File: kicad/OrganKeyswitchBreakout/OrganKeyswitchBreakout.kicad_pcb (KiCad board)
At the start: 2 copper layers, 214.4 x 52.9 mm, 114 parts, among them J1 Conn_01x16, J10 Conn_01x16, J11 Conn_01x16, J12 Conn_01x16, J13 Conn_01x16, J14 Conn_01x16, J15 CAN, J2 I2C Child, J3 CAN, J4 MIDI_OUT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

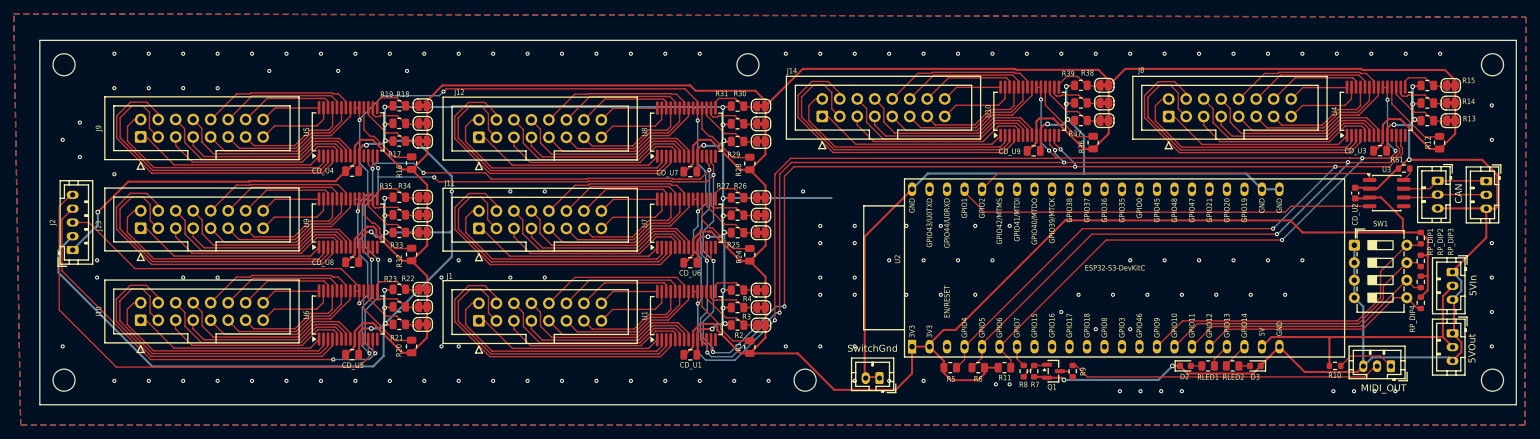
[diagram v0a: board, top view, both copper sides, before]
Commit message: Adding keyswitch breakout system, and some tools
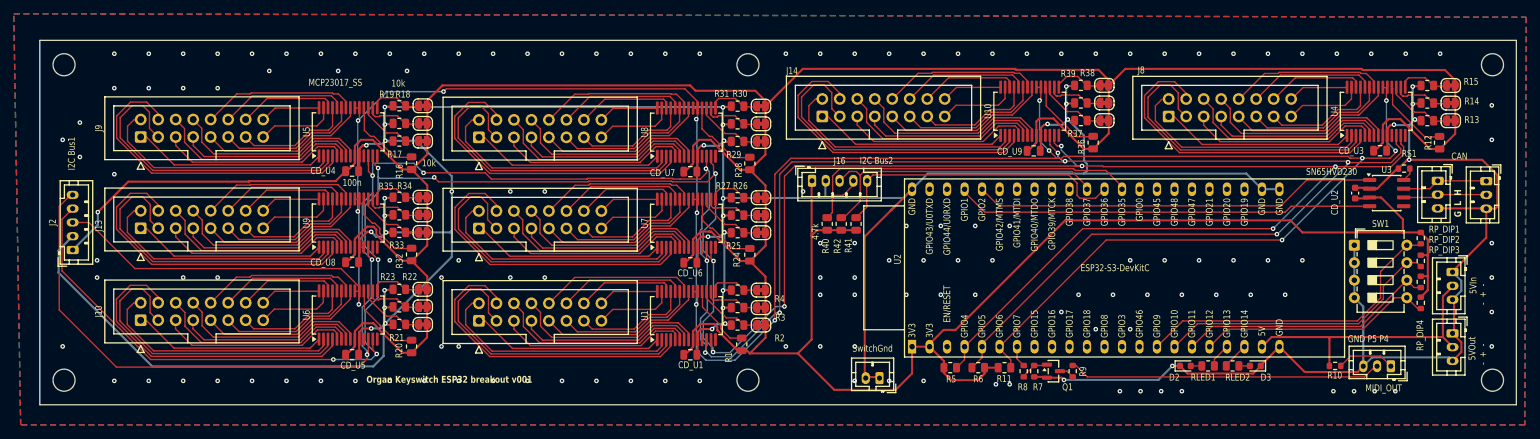
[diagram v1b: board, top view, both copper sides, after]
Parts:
- added J16: I2C Bus2, Connector_JST:JST_PH_B5B-PH-K_1x05_P2.00mm_Vertical, F.Cu at (146.3, 73.5)
- added R40: 4.7k, Resistor_SMD:R_0805_2012Metric, F.Cu at (148.5, 79.7)
- added R41: 4.7k, Resistor_SMD:R_0805_2012Metric, F.Cu at (152.7, 79.7)
- added R42: 4.7k, Resistor_SMD:R_0805_2012Metric, F.Cu at (150.5, 79.7)
- J2: value I2C Child -> I2C Bus1
- moved H4 8.30 mm to (137.0, 102.4)
- moved R1 1.24 mm to (136.1, 97.2)
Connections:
- U2 pad 32: unconnected-(U2-GPIO35-Pad32) -> /Controller/I2C_SDA2
- U2 pad 33: unconnected-(U2-GPIO36-Pad33) -> /Controller/I2C_SCL2
- U2 pad 34: unconnected-(U2-GPIO37-Pad34) -> /Controller/I2C_INT2
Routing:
- net /Controller/I2C_SDA2: track 0.00 -> 53.9 mm
- net /Controller/I2C_INT2: track 0.00 -> 46.4 mm
- net /Controller/I2C_SCL2: track 0.00 -> 43.8 mm
- net +3.3V: track 572.8 -> 605.3 mm
- net GND: track 572.5 -> 588.2 mm, vias 177 -> 173
- net SDA_IN: track 381.8 -> 386.5 mm
- net INT_INOUT: track 402.3 -> 400.1 mm
- net SCL_IN: track 388.8 -> 390.8 mm
- net Net-(U1-~{RESET}): track 11.5 -> 10.1 mm
- net /Controller/CAN/CAN_TXD: track 58.0 -> 58.8 mm
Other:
- board text added: "- + -"
- board text added: "G L H"
- board text added: "GND P5 P4"
- board text added: "Organ Keyswitch ESP32 breakout v001"
